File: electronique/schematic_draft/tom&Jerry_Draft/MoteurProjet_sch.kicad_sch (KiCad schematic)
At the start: 30 parts, among them IC1 NCS199A2RSQT2G, IC2 NCS199A2RSQT2G, J2 Conn_01x06, J3 Conn_01x06, U2 ZXBM5210-S, U3 ZXBM5210-S

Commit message: STM32 KiCAD V2 - 18.09.2024
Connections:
- net Codeur1_PH1: now also J2.3 (Pin_3); no longer J2.4 (Pin_4)
- net Codeur1_PH2: now also J2.4 (Pin_4); no longer J2.3 (Pin_3)
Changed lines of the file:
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@@
-		)
-	)
-	(global_label "PWM_MOT2_CH1"
-		(shape input)
-		(at 35.56 185.42 180)
-		(fields_autoplaced yes)
-		(effects
-			(font
-				(size 1.27 1.27)
-				(bold yes)
-			)
-			(justify right)
-		)
-		(property "Intersheetrefs" "${INTERSHEET_REFS}"
-			(at 17.3488 185.42 0)
-			(effects
-				(font
-					(size 1.27 1.27)
-				)
-				(justify right)
-				(hide yes)
-			)
-		)
-	)
-	(global_label "ADC_2"
-		(shape input)
-		(at 88.9 151.13 270)
-		(fields_autoplaced yes)
-		(effects
-			(font
-				(size 1.27 1.27)
-				(bold yes)
-			)
-			(justify right)
-		)
-		(property "Intersheetrefs" "${INTERSHEET_REFS}"
-			(at 88.9 160.2699 90)
-			(effects
-				(font
-					(size 1.27 1.27)
-				)
-				(justify right)
-				(hide yes)
-			)
-		)
-	)
-	(global_label "Codeur2_PH1"
-		(shape input)
-		(at 248.92 54.61 180)
-		(fields_autoplaced yes)
-		(effects
-			(font
-				(size 1.27 1.27)
-			)
-			(justify right)
-		)
-		(property "Intersheetrefs" "${INTERSHEET_REFS}"
-			(at 233.3559 54.61 0)
-			(effects
-				(font
-					(size 1.27 1.27)
-				)
-				(justify right)
-				(hide yes)
-			)
-		)
-	)
-	(global_label "PWM_MOT2_CH2"
-		(shape input)
-		(at 36.83 167.64 180)
-		(fields_autoplaced yes)
-		(effects
-			(font
-				(size 1.27 1.27)
-				(bold yes)
-			)
-			(justify right)
-		)
-		(property "Intersheetrefs" "${INTERSHEET_REFS}"
-			(at 18.6188 167.64 0)
-			(effects
-				(font
-					(size 1.27 1.27)
-				)
-				(justify right)
-				(hide yes)
-			)
-		)
-	)
-	(global_label "Codeur1_PH1"
-		(shape input)
-		(at 170.18 54.61 180)
-		(fields_autoplaced yes)
-		(effects
-			(font
-				(size 1.27 1.27)
-			)
-			(justify right)
-		)
-		(property "Intersheetrefs" "${INTERSHEET_REFS}"
-			(at 154.6159 54.61 0)
-			(effects
-				(font
-					(size 1.27 1.27)
-				)
-				(justify right)
-				(hide yes)
-			)
-		)
-	)
-	(global_label "PWM_MOT2_CH2"
-		(shape input)
-		(at 35.56 194.31 180)
-		(fields_autoplaced yes)
-		(effects
-			(font
-				(size 1.27 1.27)
-				(bold yes)
-			)
-			(justify right)
-		)
-		(property "Intersheetrefs" "${INTERSHEET_REFS}"
-			(at 17.3488 194.31 0)
-			(effects
-				(font
-					(size 1.27 1.27)
-				)
-				(justify right)
-				(hide yes)
-			)
-		)
-	)
-	(global_label "PWM_MOT2_CH1"
-		(shape input)
-		(at 36.83 165.1 180)
-		(fields_autoplaced yes)
-		(effects
-			(font
-				(size 1.27 1.27)
-				(bold yes)
-			)
-			(justify right)
-		)
-		(property "Intersheetrefs" "${INTERSHEET_REFS}"
-			(at 18.6188 165.1 0)
-			(effects
-				(font
-					(size 1.27 1.27)
-				)
-				(justify right)
-				(hide yes)
-			)
-		)
-	)
-	(global_label "Codeur2_PH2"
-		(shape input)
-		(at 248.92 57.15 180)
-		(fields_autoplaced yes)
-		(effects
-			(font
-				(size 1.27 1.27)
-			)
-			(justify right)
-		)
-		(property "Intersheetrefs" "${INTERSHEET_REFS}"
-			(at 233.3559 57.15 0)
-			(effects
-				(font
-					(size 1.27 1.27)
-				)
-				(justify right)
-				(hide yes)
-			)
-		)
-	)
-	(global_label "PWM_MOT1_CH2"
-		(shape input)
-		(at 19.05 33.02 90)
-		(fields_autoplaced yes)
-		(effects
-			(font
-				(size 1.27 1.27)
-				(bold yes)
-			)
-			(justify left)
-		)
-		(property "Intersheetrefs" "${INTERSHEET_REFS}"
-			(at 19.05 14.8088 90)
-			(effects
-				(font
-					(size 1.27 1.27)
-				)
-				(justify left)
-				(hide yes)
-			)
-		)
-	)
-	(global_label "Codeur1_PH2"
-		(shape input)
-		(at 170.18 52.07 180)
-		(fields_autoplaced yes)
-		(effects
-			(font
-				(size 1.27 1.27)
-			)
-			(justify right)
-		)
-		(property "Intersheetrefs" "${INTERSHEET_REFS}"
-			(at 154.6159 52.07 0)
-			(effects
-				(font
-					(size 1.27 1.27)
-				)
-				(justify right)
-				(hide yes)
-			)
-		)
-	)
-	(global_label "PWM_MOT1_CH1"
-		(shape input)
-		(at 34.29 74.93 180)
-		(fields_autoplaced yes)
-		(effects
-			(font
-				(size 1.27 1.27)
-				(bold yes)
-			)
-			(justify right)
-		)
-		(property "Intersheetrefs" "${INTERSHEET_REFS}"
-			(at 16.0788 74.93 0)
-			(effects
-				(font
-					(size 1.27 1.27)
-				)
-				(justify right)
-				(hide yes)
-			)
 		)
 	)
@@
 		)
 	)
-	(global_label "PWM_MOT1_CH1"
+	(hierarchical_label "Codeur1_PH2"
+		(shape input)
+		(at 170.18 54.61 180)
+		(fields_autoplaced yes)
+		(effects
+			(font
+				(size 1.27 1.27)
+			)
+			(justify right)
+		)
+	)
+	(hierarchical_label "Codeur2_PH2"
+		(shape input)
+		(at 248.92 57.15 180)
+		(fields_autoplaced yes)
+		(effects
+			(font
+				(size 1.27 1.27)
+			)
+			(justify right)
+		)
+	)
+	(hierarchical_label "PWM_MOT2_CH2"
+		(shape input)
+		(at 36.83 167.64 180)
+		(fields_autoplaced yes)
+		(effects
+			(font
+				(size 1.27 1.27)
+				(bold yes)
+			)
+			(justify right)
+		)
+	)
+	(hierarchical_label "PWM_MOT2_CH2"
+		(shape input)
+		(at 35.56 194.31 180)
+		(fields_autoplaced yes)
+		(effects
+			(font
+				(size 1.27 1.27)
+				(bold yes)
+			)
+			(justify right)
+		)
+	)
+	(hierarchical_label "PWM_MOT1_CH2"
+		(shape input)
+		(at 19.05 33.02 90)
+		(fields_autoplaced yes)
+		(effects
+			(font
+				(size 1.27 1.27)
+				(bold yes)
+			)
+			(justify left)
+		)
+	)
+	(hierarchical_label "PWM_MOT1_CH2"
+		(shape input)
+		(at 34.29 77.47 180)
+		(fields_autoplaced yes)
+		(effects
+			(font
+				(size 1.27 1.27)
+				(bold yes)
+			)
+			(justify right)
+		)
+	)
+	(hierarchical_label "ADC_2"
+		(shape input)
+		(at 88.9 151.13 270)
+		(fields_autoplaced yes)
+		(effects
+			(font
+				(size 1.27 1.27)
+				(bold yes)
+			)
+			(justify right)
+		)
+	)
+	(hierarchical_label "Codeur2_PH1"
+		(shape input)
+		(at 248.92 54.61 180)
+		(fields_autoplaced yes)
+		(effects
+			(font
+				(size 1.27 1.27)
+			)
+			(justify right)
+		)
+	)
+	(hierarchical_label "PWM_MOT1_CH1"
 		(shape input)
 		(at 27.94 33.02 90)
@@
 			(justify left)
 		)
-		(property "Intersheetrefs" "${INTERSHEET_REFS}"
-			(at 27.94 14.8088 90)
-			(effects
-				(font
-					(size 1.27 1.27)
-				)
-				(justify left)
-				(hide yes)
-			)
-		)
 	)
-	(global_label "PWM_MOT1_CH2"
+	(hierarchical_label "PWM_MOT2_CH1"
 		(shape input)
-		(at 34.29 77.47 180)
+		(at 35.56 185.42 180)
 		(fields_autoplaced yes)
 		(effects
@@
 			(justify right)
 		)
-		(property "Intersheetrefs" "${INTERSHEET_REFS}"
-			(at 16.0788 77.47 0)
-			(effects
-				(font
-					(size 1.27 1.27)
-				)
-				(justify right)
-				(hide yes)
+	)
+	(hierarchical_label "PWM_MOT2_CH1"
+		(shape input)
+		(at 36.83 165.1 180)
+		(fields_autoplaced yes)
+		(effects
+			(font
+				(size 1.27 1.27)
+				(bold yes)
 			)
+			(justify right)
 		)
 	)
+	(hierarchical_label "PWM_MOT1_CH1"
+		(shape input)
+		(at 34.29 74.93 180)
+		(fields_autoplaced yes)
+		(effects
+			(font
+				(size 1.27 1.27)
+				(bold yes)
+			)
+			(justify right)
+		)
+	)
+	(hierarchical_label "Codeur1_PH1"
+		(shape input)
+		(at 170.18 52.07 180)
+		(fields_autoplaced yes)
+		(effects
+			(font
+				(size 1.27 1.27)
+			)
+			(justify right)
+		)
+	)

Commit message: STM32 KiCAD V4 - 20.09.2024
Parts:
- removed C16, C21, C22: 1uF, Capacitor_SMD:C_0603_1608Metric_Pad1.08x0.95mm_HandSolder, symbol Device:C_Small
- removed C18: 10uF, Capacitor_SMD:C_0603_1608Metric_Pad1.08x0.95mm_HandSolder, symbol Device:C_Small
- removed C24, C25: 100nF, Capacitor_SMD:C_0603_1608Metric_Pad1.08x0.95mm_HandSolder, symbol Device:C_Small
- removed D10, D11, D8, D9: RED, LED_SMD:LED_0603_1608Metric_Pad1.05x0.95mm_HandSolder, symbol Device:LED_Small
- removed IC2: NCS199A2RSQT2G, Library:SOT65P210X110-6N, symbol Ludzlib:NCS199A2RSQT2G
- removed R14, R15, R16, R17: 390R, Resistor_SMD:R_0603_1608Metric_Pad0.98x0.95mm_HandSolder, symbol Device:R_Small
- removed R19: 0.015, Resistor_SMD:R_1206_3216Metric_Pad1.30x1.75mm_HandSolder, symbol Device:R_Small
- removed U3: ZXBM5210-S, Package_SO:SOIC-8-1EP_3.9x4.9mm_P1.27mm_EP2.62x3.51mm_ThermalVias, symbol Driver_Motor:ZXBM5210-S
- added D401, D402, D403, D404: RED, LED_SMD:LED_0603_1608Metric_Pad1.05x0.95mm_HandSolder, symbol Device:LED_Small
- added R401: 1k, symbol Device:R_Small
- added R403, R404, R405, R406: 390R, Resistor_SMD:R_0603_1608Metric_Pad0.98x0.95mm_HandSolder, symbol Device:R_Small
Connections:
- net GND: now also R403.2, R404.2, R405.2, R406.2
- net PWM_MOT1_CH1: now also D402.2 (A)
- net PWM_MOT1_CH2: now also D401.2 (A)
- net PWM_MOT2_CH1: now also D403.2 (A)
- net PWM_MOT2_CH2: now also D404.2 (A)
- net REF: now also R401.2
- net ADC_1 renamed Out_CurrMeas1
- net Out_CurrMeas1: now also R401.1
- new net: D401.1 (K), R403.1
- new net: D402.1 (K), R404.1
- new net: D403.1 (K), R405.1
- new net: D404.1 (K), R406.1
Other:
- added sheet Motor Driver (MotorDriver.kicad_sch)
- note added: "Frequence du PWM de 10kHZ, pas sure que les LEDS tiennent la frequence"
- note removed: "Shunt resistor"
- note removed: "recommended capacitance is 100nF to 10μF"
- moved on the sheet: C26, R20, R21

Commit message: STM32 KiCAD V5 - 20.09.2024
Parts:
- removed C15, C19, C20: 1uF, Capacitor_SMD:C_0603_1608Metric_Pad1.08x0.95mm_HandSolder, symbol Device:C_Small
- removed C17: 10uF, Capacitor_SMD:C_0603_1608Metric_Pad1.08x0.95mm_HandSolder, symbol Device:C_Small
- removed C23: 100nF, Capacitor_SMD:C_0603_1608Metric_Pad1.08x0.95mm_HandSolder, symbol Device:C_Small
- removed D401, D402, D403, D404: RED, LED_SMD:LED_0603_1608Metric_Pad1.05x0.95mm_HandSolder, symbol Device:LED_Small
- removed IC1: NCS199A2RSQT2G, Library:SOT65P210X110-6N, symbol Ludzlib:NCS199A2RSQT2G
- removed R18: 0.015, Resistor_SMD:R_1206_3216Metric_Pad1.30x1.75mm_HandSolder, symbol Device:R_Small
- removed R401: 1k, symbol Device:R_Small
- removed R403, R404, R405, R406: 390R, Resistor_SMD:R_0603_1608Metric_Pad0.98x0.95mm_HandSolder, symbol Device:R_Small
- removed U2: ZXBM5210-S, Package_SO:SOIC-8-1EP_3.9x4.9mm_P1.27mm_EP2.62x3.51mm_ThermalVias, symbol Driver_Motor:ZXBM5210-S
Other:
- sheet Motor Driver renamed Motor Driver 1
- added sheet Motor Driver 2 (MotorDriver.kicad_sch)
- sheet Motor Driver 1 ports: added Motor+, Motor-, Out_CurrMeas, PWM_MOTx_CH1, PWM_MOTx_CH2, REF; removed none
- note removed: "Frequence du PWM de 10kHZ, pas sure que les LEDS tiennent la frequence"
- note removed: "Gain 100"
- note removed: "Motor driver 1"
- note removed: "Motor driver 2"
- note removed: "R405 : 3A -> max current -> 3V(out) 3V/200=0.015V So R=0.015 P=RI^2 P=0.135W 1206 OK"
- note removed: "recommended capacitance is 100nF to 1μF"
- moved on the sheet: C26, J2, J3, R20, R21

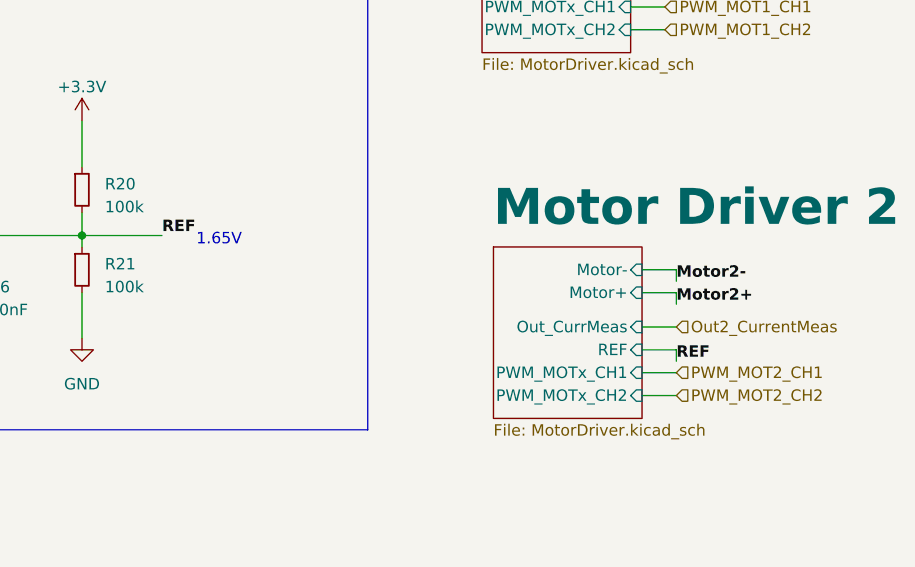
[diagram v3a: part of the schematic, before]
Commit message: STM32 KiCAD V6 - 25.09.2024 - Ajout des points test
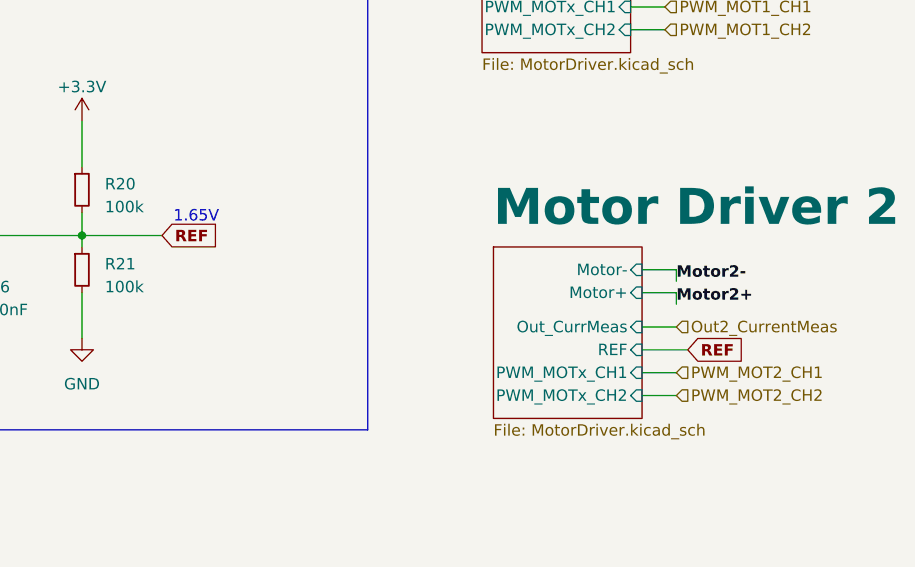
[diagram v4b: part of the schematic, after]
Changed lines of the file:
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@@
 	(wire
 		(pts
-			(xy 152.4 119.38) (xy 148.59 119.38)
-		)
-		(stroke
-			(width 0)
-			(type default)
-		)
-	)
-	(wire
-		(pts
-			(xy 152.4 119.38) (xy 152.4 120.65)
+			(xy 153.67 119.38) (xy 148.59 119.38)
 		)
 		(stroke
@@
 	(text "1.65V"
 		(exclude_from_sim no)
-		(at 99.06 107.95 0)
+		(at 96.52 105.41 0)
 		(effects
 			(font
@@
 		)
 	)
-	(label "REF"
-		(at 152.4 120.65 0)
-		(fields_autoplaced yes)
-		(effects
-			(font
-				(size 1.27 1.27)
-				(bold yes)
-			)
-			(justify left bottom)
-		)
-	)
 	(label "Motor1+"
 		(at 240.03 86.36 0)
@@
 		)
 	)
-	(label "REF"
-		(at 95.25 106.68 0)
-		(fields_autoplaced yes)
-		(effects
-			(font
-				(size 1.27 1.27)
-				(bold yes)
-			)
-			(justify left bottom)
-		)
-	)
 	(label "Motor1-"
 		(at 241.3 73.66 0)
@@
 		)
 	)
+	(global_label "REF"
+		(shape input)
+		(at 95.25 106.68 0)
+		(fields_autoplaced yes)
+		(effects
+			(font
+				(size 1.27 1.27)
+				(bold yes)
+			)
+			(justify left)
+		)
+		(property "Intersheetrefs" "${INTERSHEET_REFS}"
+			(at 102.2188 106.68 0)
+			(effects
+				(font
+					(size 1.27 1.27)
+				)
+				(justify left)
+				(hide yes)
+			)
+		)
+	)
+	(global_label "REF"
+		(shape input)
+		(at 153.67 119.38 0)
+		(fields_autoplaced yes)
+		(effects
+			(font
+				(size 1.27 1.27)
+				(bold yes)
+			)
+			(justify left)
+		)
+		(property "Intersheetrefs" "${INTERSHEET_REFS}"
+			(at 160.6388 119.38 0)
+			(effects
+				(font
+					(size 1.27 1.27)
+				)
+				(justify left)
+				(hide yes)
+			)
+		)
+	)

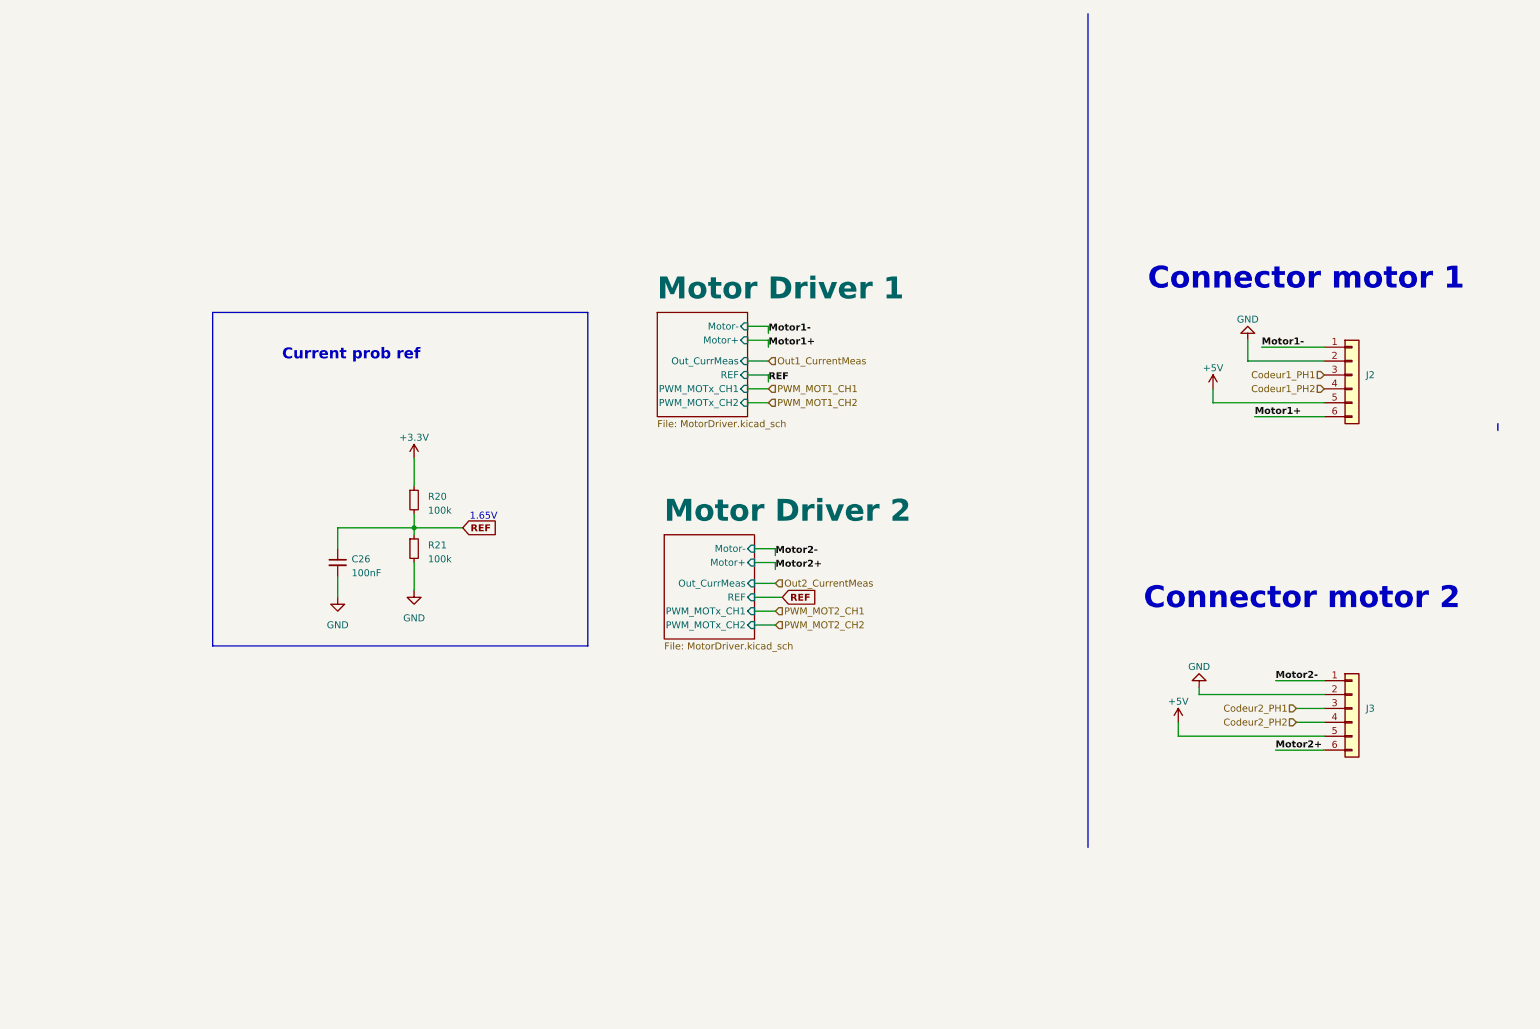
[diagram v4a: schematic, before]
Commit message: STM32 KiCAD v2.0 x CubeIDE - Pin definitif + schematic reviewed
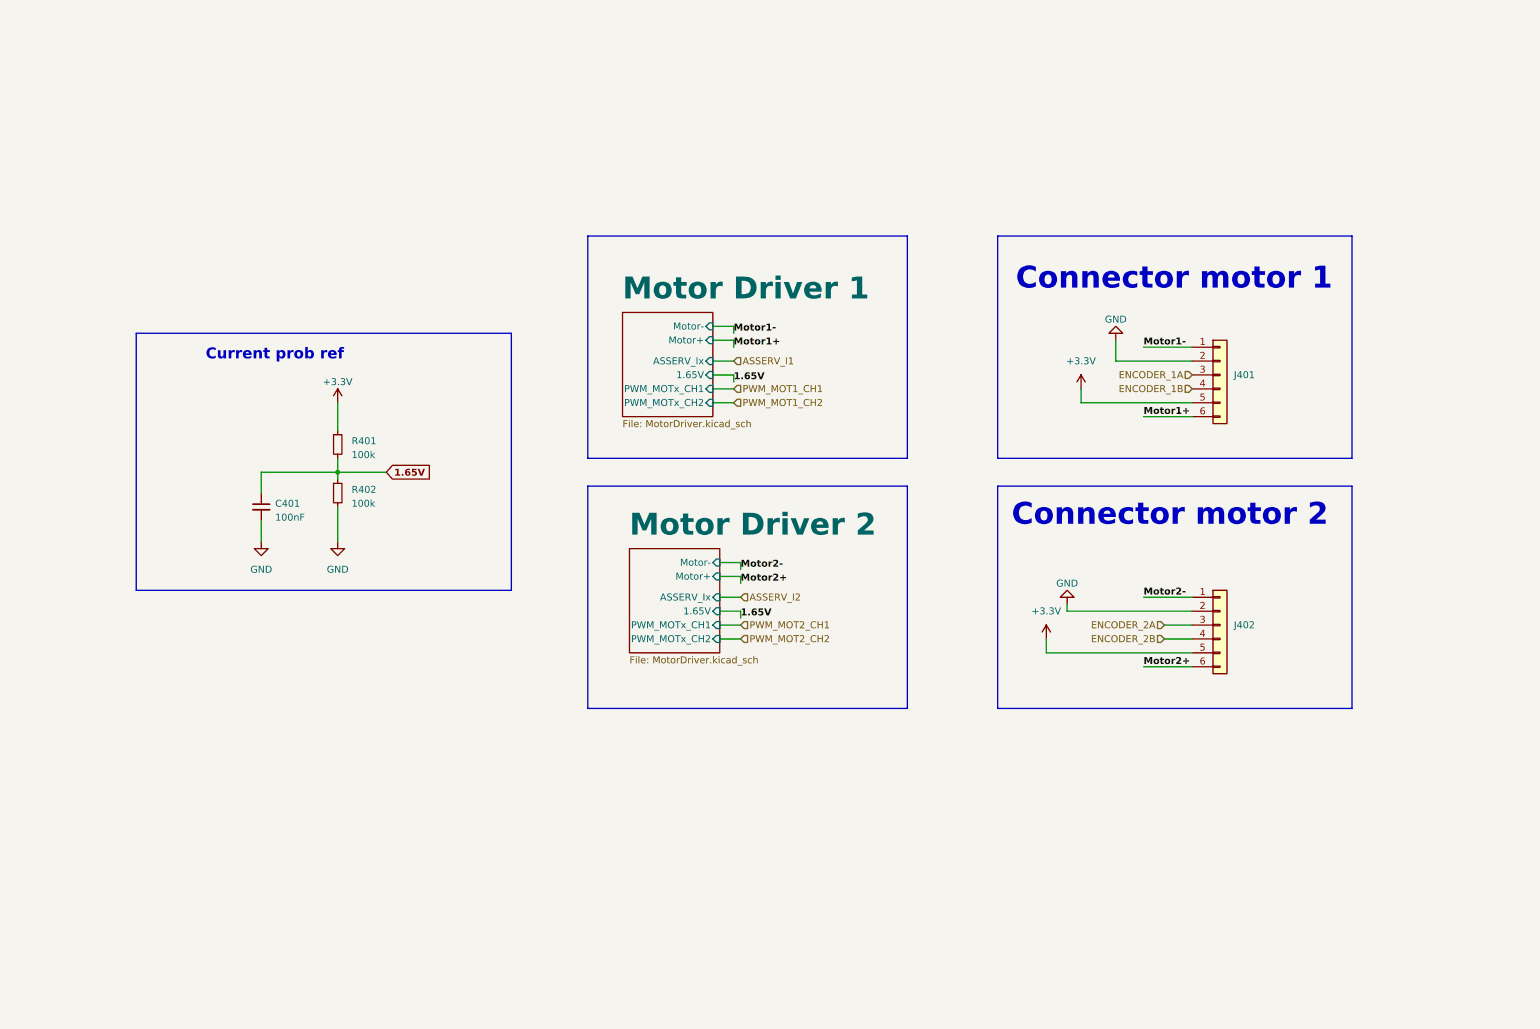
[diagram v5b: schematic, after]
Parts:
- renumbered C26 to C401, J2 to J401, J3 to J402, R20 to R401, R21 to R402
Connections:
- net +5V is gone; now on net +3.3V: J401.5 (Pin_5), J402.5 (Pin_5)
- net Codeur1_PH1 renamed ENCODER_1A
- net Codeur1_PH2 renamed ENCODER_1B
- net Codeur2_PH1 renamed ENCODER_2A
- net Codeur2_PH2 renamed ENCODER_2B
- net REF renamed 1.65V
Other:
- sheet Motor Driver 1 ports: added 1.65V, ASSERV_Ix; removed Out_CurrMeas, REF
- sheet Motor Driver 2 ports: added 1.65V, ASSERV_Ix; removed Out_CurrMeas, REF
- note removed: "1.65V"
- moved on the sheet: C401, J401, J402, R401, R402

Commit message: Adding footprint V0.1
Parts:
- C401: footprint Capacitor_SMD:C_0603_1608Metric_Pad1.08x0.95mm_HandSolder -> Capacitor_SMD:C_0402_1005Metric
- R401, R402: footprint Resistor_SMD:R_0603_1608Metric_Pad0.98x0.95mm_HandSolder -> Resistor_SMD:R_0402_1005Metric
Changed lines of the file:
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@@
 			)
 		)
-		(property "Footprint" "Resistor_SMD:R_0603_1608Metric_Pad0.98x0.95mm_HandSolder"
+		(property "Footprint" "Resistor_SMD:R_0402_1005Metric"
 			(at 72.39 100.33 0)
 			(effects
@@
 			)
 		)
-		(property "Footprint" "Capacitor_SMD:C_0603_1608Metric_Pad1.08x0.95mm_HandSolder"
+		(property "Footprint" "Capacitor_SMD:C_0402_1005Metric"
 			(at 58.42 102.87 0)
 			(effects
@@
 			)
 		)
-		(property "Footprint" "Resistor_SMD:R_0603_1608Metric_Pad0.98x0.95mm_HandSolder"
+		(property "Footprint" "Resistor_SMD:R_0402_1005Metric"
 			(at 72.39 91.44 0)
 			(effects
